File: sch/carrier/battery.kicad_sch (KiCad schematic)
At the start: 2 parts

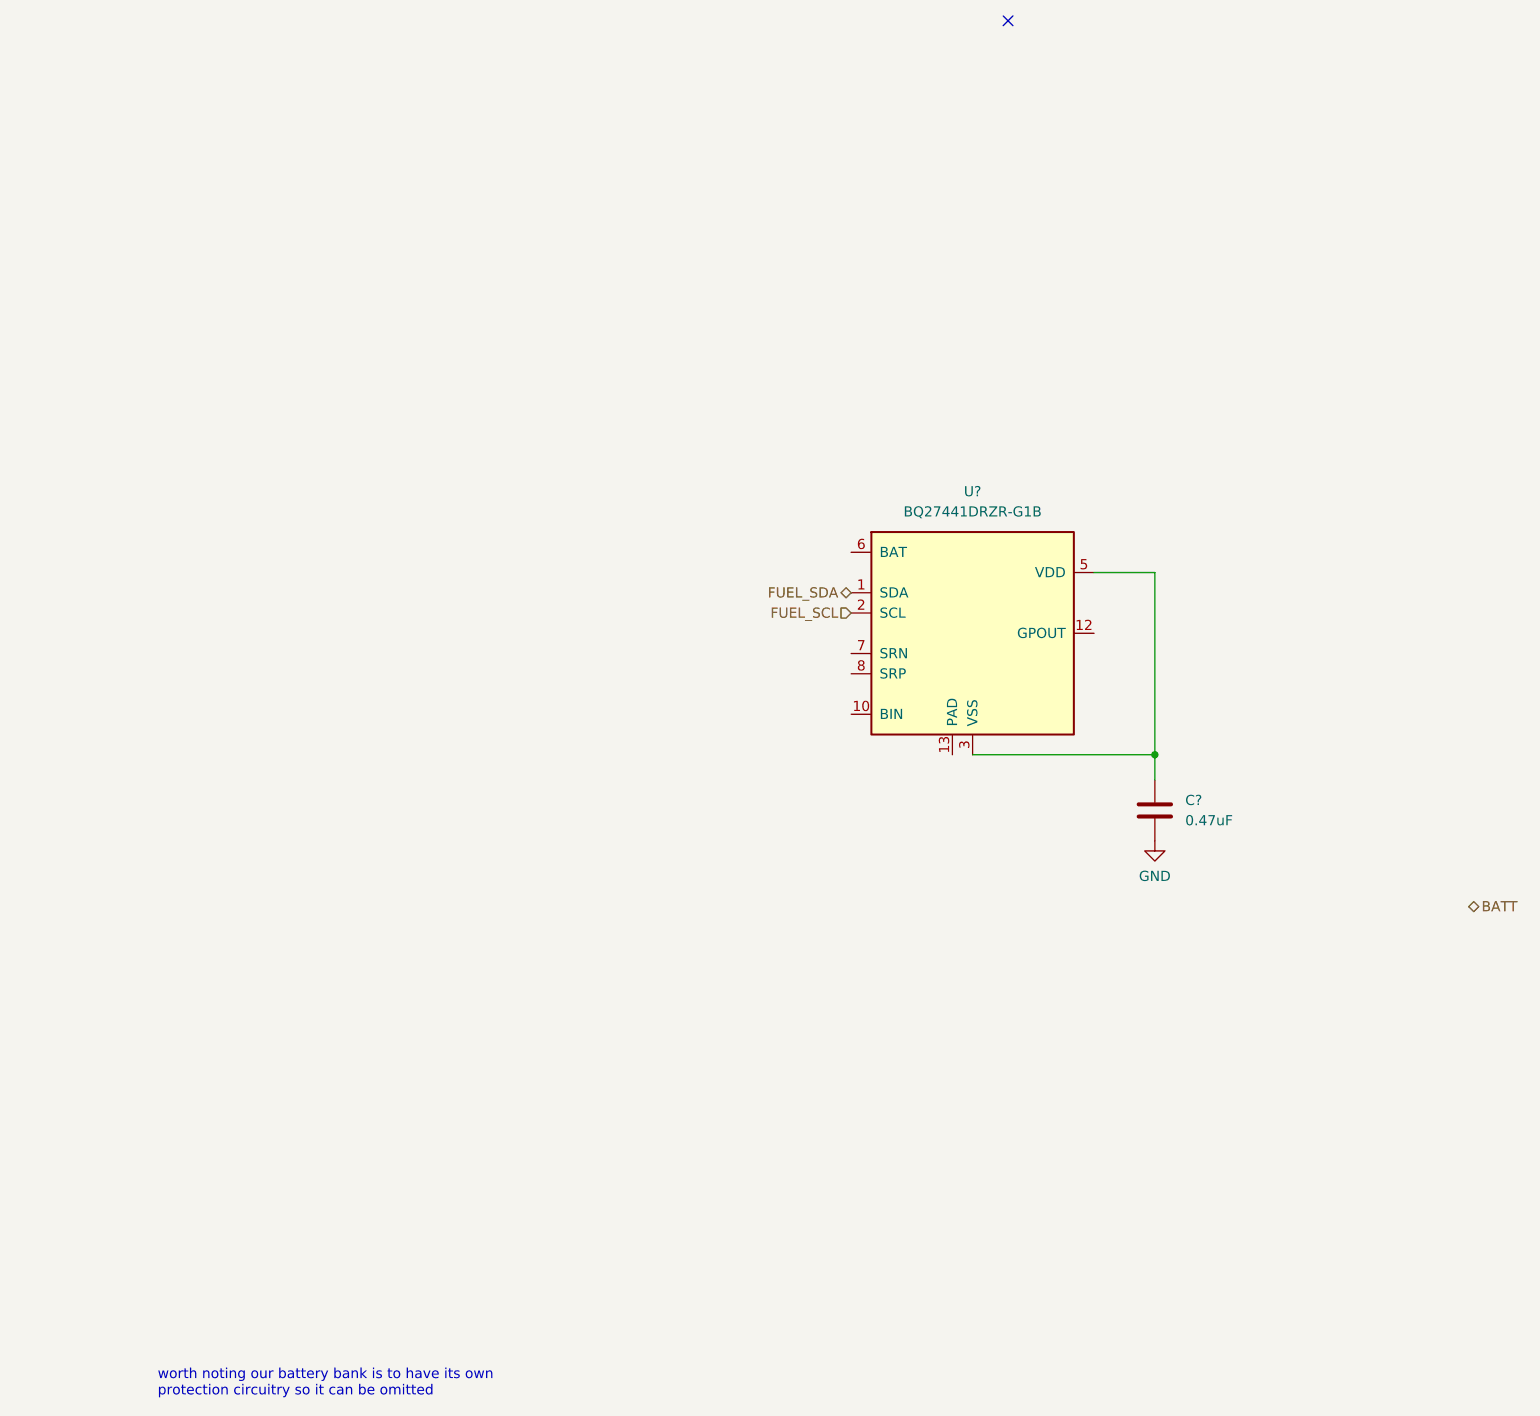
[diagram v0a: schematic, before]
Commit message: add speaker and charger
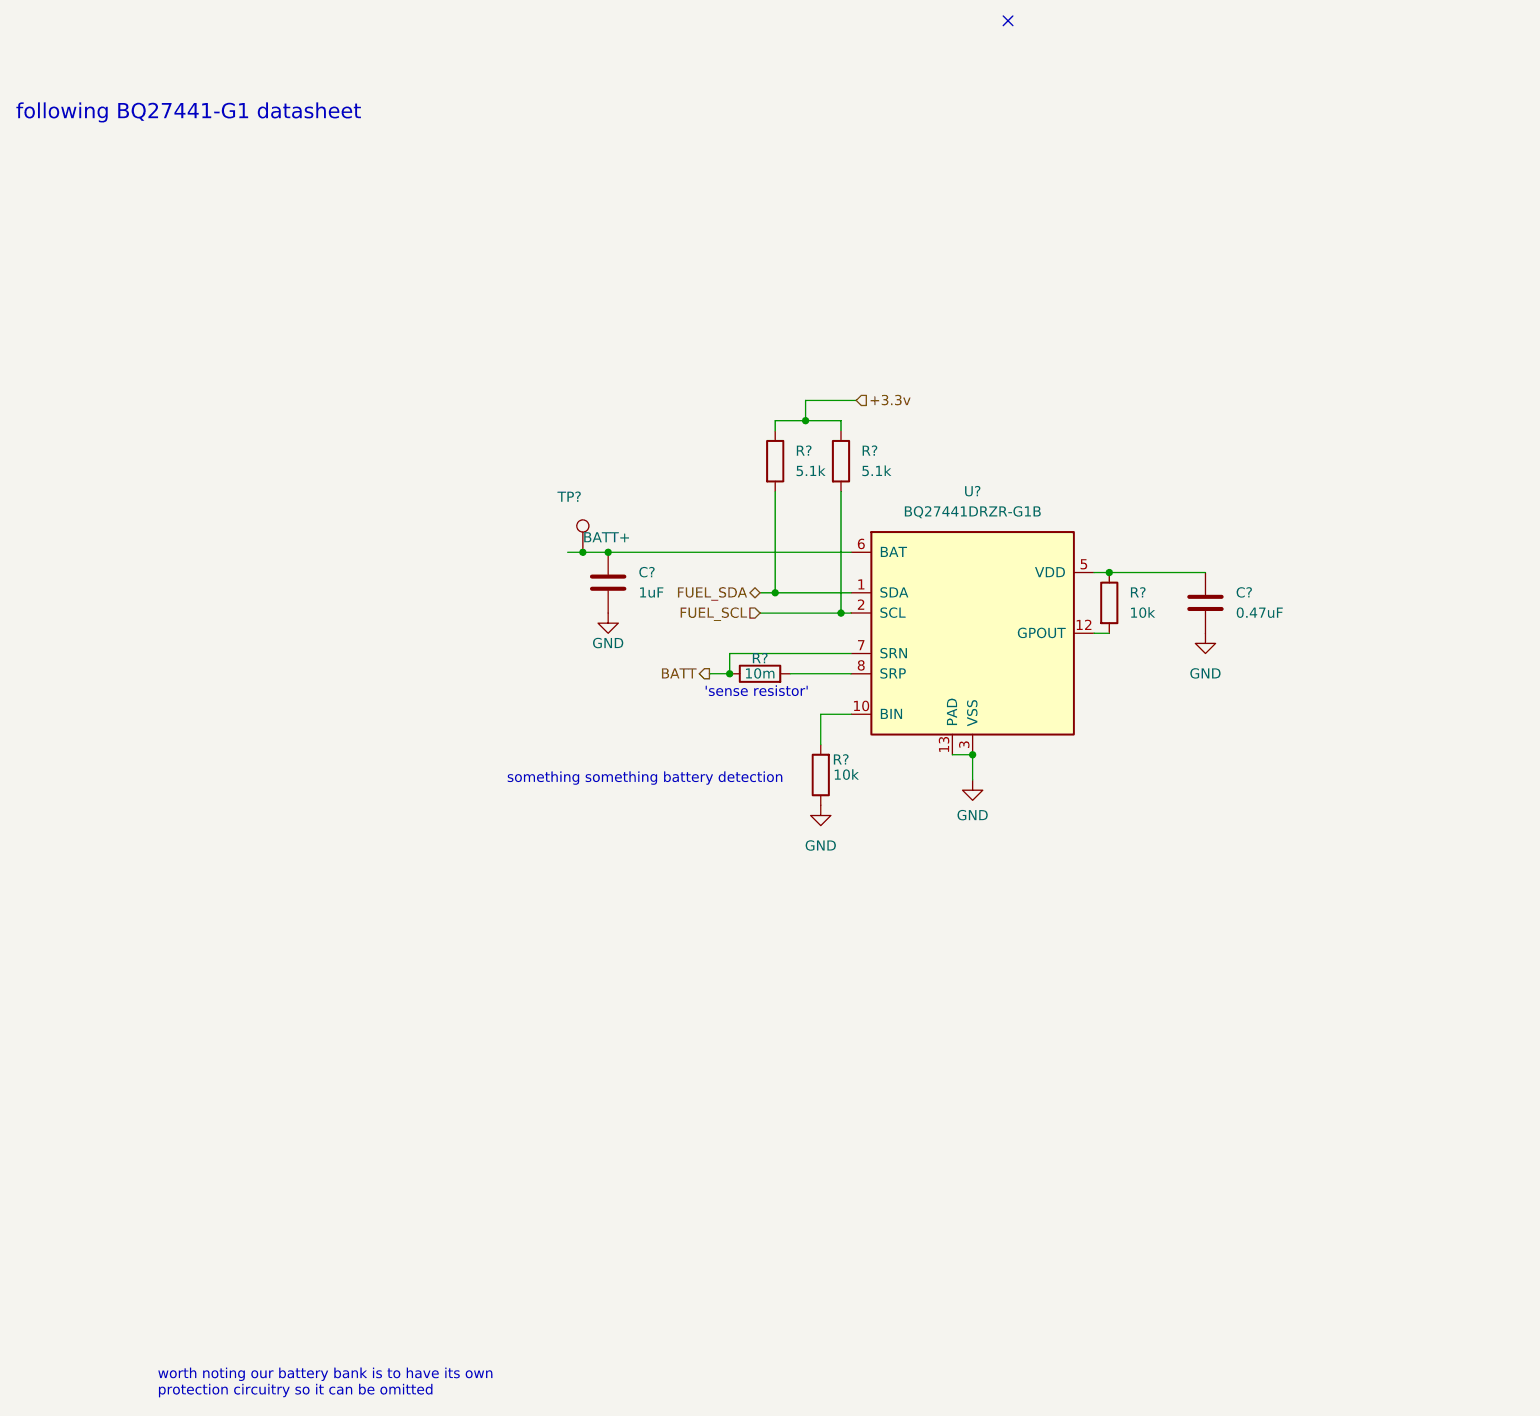
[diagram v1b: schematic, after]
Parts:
- added C?: 1uF, symbol Device:C
- added R? (x2): 5.1k, symbol Device:R
- added R?: 10m, symbol Device:R
- added R? (x2): 10k, symbol Device:R
- added TP?: BATT+, symbol Connector:TestPoint
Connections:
- net BATT: now also U?.7 (SRN), R?.1
- net FUEL_SCL: now also R?.2
- net FUEL_SDA: now also R?.2
- net GND: now also U?.13 (PAD), U?.3 (VSS), C?.2, R?.1
- net at C?.1, U?.5 (VDD): now also R?.1; no longer U?.3 (VSS)
- net at U?.10 (BIN): now also R?.2
- net at U?.12 (GPOUT): now also R?.2
- net at U?.6 (BAT): now also C?.1, TP?.1
- net at U?.8 (SRP): now also R?.2
- new net +3.3v: R?.1, R?.1
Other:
- note added: "'sense resistor'"
- note added: "following BQ27441-G1 datasheet"
- note added: "something something battery detection"
- moved on the sheet: C?

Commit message: push updates
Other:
- moved on the sheet: TP?
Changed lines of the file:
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@@
     (comment 1 "https://www.github.com/cinnamondev/gamepithing")
   )
-  (junction (at 92.71 72.39) (diameter 0.9144) (color 0 0 0 0))
+  (junction (at 92.075 72.39) (diameter 0.9144) (color 0 0 0 0))
   (junction (at 95.885 72.39) (diameter 0.9144) (color 0 0 0 0))
   (junction (at 111.125 87.63) (diameter 0.9144) (color 0 0 0 0))
@@
   (junction (at 158.75 74.93) (diameter 0.9144) (color 0 0 0 0))
   (no_connect (at 146.05 5.715))
-  (wire (pts (xy 90.805 72.39) (xy 92.71 72.39))
+  (wire (pts (xy 90.805 72.39) (xy 92.075 72.39))
     (stroke (width 0) (type solid) (color 0 0 0 0))
   )
-  (wire (pts (xy 92.71 72.39) (xy 95.885 72.39))
+  (wire (pts (xy 92.075 72.39) (xy 95.885 72.39))
     (stroke (width 0) (type solid) (color 0 0 0 0))
   )
@@
     (effects (font (size 1.27 1.27)) (justify left))
   )
-  (symbol (lib_id "Connector:TestPoint") (at 92.71 72.39 0) (unit 1)
+  (symbol (lib_id "Connector:TestPoint") (at 92.075 72.39 0) (unit 1)
     (in_bom yes) (on_board yes)
-    (property "Reference" "TP?" (id 0) (at 89.535 65.4684 0)
+    (property "Reference" "TP?" (id 0) (at 88.9 65.4684 0)
       (effects (font (size 1.27 1.27)) (justify left))
     )
-    (property "Value" "BATT+" (id 1) (at 92.71 70.5484 0)
+    (property "Value" "BATT+" (id 1) (at 92.075 70.5484 0)
       (effects (font (size 1.27 1.27)) (justify left))
     )
-    (property "Footprint" "" (id 2) (at 97.79 72.39 0)
+    (property "Footprint" "" (id 2) (at 97.155 72.39 0)
       (effects (font (size 1.27 1.27)) hide)
     )
-    (property "Datasheet" "~" (id 3) (at 97.79 72.39 0)
+    (property "Datasheet" "~" (id 3) (at 97.155 72.39 0)
       (effects (font (size 1.27 1.27)) hide)
     )

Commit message: git pushed
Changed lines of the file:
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@@
     (title "Power and battery")
     (rev "indev")
-    (comment 1 "https://www.github.com/cinnamondev/gamepithing")
   )
   (junction (at 92.075 72.39) (diameter 0.9144) (color 0 0 0 0))
@@
     (effects (font (size 1.27 1.27)) (justify left bottom))
   )
-  (hierarchical_label "BATT" (shape output) (at 108.585 87.63 180)
+  (hierarchical_label "BATT" (shape bidirectional) (at 108.585 87.63 180)
     (effects (font (size 1.27 1.27)) (justify right))
   )

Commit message: we're abt ready to do pcb i hope!
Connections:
- net BATT: now also R?.2; no longer R?.1
- net at C?.1, TP?.1, U?.6 (BAT): now also R?.1, U?.8 (SRP)
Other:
- moved on the sheet: R?
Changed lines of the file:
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@@
   (junction (at 92.075 72.39) (diameter 0.9144) (color 0 0 0 0))
   (junction (at 95.885 72.39) (diameter 0.9144) (color 0 0 0 0))
-  (junction (at 111.125 87.63) (diameter 0.9144) (color 0 0 0 0))
+  (junction (at 103.505 72.39) (diameter 0.9144) (color 0 0 0 0))
+  (junction (at 110.49 85.09) (diameter 0.9144) (color 0 0 0 0))
+  (junction (at 110.49 92.71) (diameter 0.9144) (color 0 0 0 0))
   (junction (at 116.84 77.47) (diameter 0.9144) (color 0 0 0 0))
   (junction (at 120.65 55.88) (diameter 0.9144) (color 0 0 0 0))
@@
     (stroke (width 0) (type solid) (color 0 0 0 0))
   )
-  (wire (pts (xy 95.885 72.39) (xy 126.365 72.39))
-    (stroke (width 0) (type solid) (color 0 0 0 0))
-  )
-  (wire (pts (xy 108.585 87.63) (xy 111.125 87.63))
-    (stroke (width 0) (type solid) (color 0 0 0 0))
-  )
-  (wire (pts (xy 111.125 85.09) (xy 111.125 87.63))
+  (wire (pts (xy 95.885 72.39) (xy 103.505 72.39))
+    (stroke (width 0) (type solid) (color 0 0 0 0))
+  )
+  (wire (pts (xy 103.505 72.39) (xy 126.365 72.39))
+    (stroke (width 0) (type solid) (color 0 0 0 0))
+  )
+  (wire (pts (xy 103.505 92.71) (xy 103.505 72.39))
+    (stroke (width 0) (type solid) (color 0 0 0 0))
+  )
+  (wire (pts (xy 109.855 85.09) (xy 110.49 85.09))
+    (stroke (width 0) (type solid) (color 0 0 0 0))
+  )
+  (wire (pts (xy 110.49 85.09) (xy 126.365 85.09))
+    (stroke (width 0) (type solid) (color 0 0 0 0))
+  )
+  (wire (pts (xy 110.49 92.71) (xy 103.505 92.71))
     (stroke (width 0) (type solid) (color 0 0 0 0))
   )
@@
     (stroke (width 0) (type solid) (color 0 0 0 0))
   )
-  (wire (pts (xy 118.745 87.63) (xy 126.365 87.63))
+  (wire (pts (xy 118.745 87.63) (xy 118.745 92.71))
+    (stroke (width 0) (type solid) (color 0 0 0 0))
+  )
+  (wire (pts (xy 118.745 92.71) (xy 110.49 92.71))
     (stroke (width 0) (type solid) (color 0 0 0 0))
   )
@@
     (stroke (width 0) (type solid) (color 0 0 0 0))
   )
-  (wire (pts (xy 126.365 85.09) (xy 111.125 85.09))
+  (wire (pts (xy 126.365 87.63) (xy 118.745 87.63))
     (stroke (width 0) (type solid) (color 0 0 0 0))
   )
@@
     (effects (font (size 1.27 1.27)) (justify left bottom))
   )
-  (text "'sense resistor'" (at 107.95 90.805 0)
+  (text "'sense resistor'" (at 97.79 96.52 0)
     (effects (font (size 1.27 1.27)) (justify left bottom))
   )
-  (hierarchical_label "BATT" (shape bidirectional) (at 108.585 87.63 180)
+  (hierarchical_label "BATT" (shape bidirectional) (at 109.855 85.09 180)
     (effects (font (size 1.27 1.27)) (justify right))
   )
@@
     (pin "1")
   )
-  (symbol (lib_id "Device:R") (at 114.935 87.63 90) (unit 1)
+  (symbol (lib_id "Device:R") (at 110.49 88.9 180) (unit 1)
     (in_bom yes) (on_board yes)
-    (property "Reference" "R?" (id 0) (at 114.935 85.725 90))
-    (property "Value" "10m" (id 1) (at 114.935 87.63 90))
-    (property "Footprint" "" (id 2) (at 114.935 89.408 90)
-      (effects (font (size 1.27 1.27)) hide)
-    )
-    (property "Datasheet" "~" (id 3) (at 114.935 87.63 0)
-      (effects (font (size 1.27 1.27)) hide)
-    )
+    (property "Reference" "R?" (id 0) (at 108.585 88.9 90))
+    (property "Value" "10m" (id 1) (at 110.49 88.9 90))
+    (property "Footprint" "" (id 2) (at 112.268 88.9 90)
+      (effects (font (size 1.27 1.27)) hide)
+    )
+    (property "Datasheet" "~" (id 3) (at 110.49 88.9 0)
+      (effects (font (size 1.27 1.27)) hide)
+    )

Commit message: ersfdxcv
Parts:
- TP26: renamed from TP?; footprint (none) -> TestPoint:TestPoint_Pad_1.0x1.0mm
- gave numbers to parts that had none: 8
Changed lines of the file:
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@@
   (symbol (lib_id "Connector:TestPoint") (at 92.075 72.39 0) (unit 1)
     (in_bom yes) (on_board yes)
-    (property "Reference" "TP?" (id 0) (at 88.9 65.4684 0)
+    (property "Reference" "TP26" (id 0) (at 88.9 65.4684 0)
       (effects (font (size 1.27 1.27)) (justify left))
     )
@@
       (effects (font (size 1.27 1.27)) (justify left))
     )
-    (property "Footprint" "" (id 2) (at 97.155 72.39 0)
+    (property "Footprint" "TestPoint:TestPoint_Pad_1.0x1.0mm" (id 2) (at 97.155 72.39 0)
       (effects (font (size 1.27 1.27)) hide)
     )
@@
   (symbol (lib_id "power:GND") (at 95.885 80.01 0) (unit 1)
     (in_bom yes) (on_board yes)
-    (property "Reference" "#PWR?" (id 0) (at 95.885 86.36 0)
+    (property "Reference" "#PWR048" (id 0) (at 95.885 86.36 0)
       (effects (font (size 1.27 1.27)) hide)
     )
@@
   (symbol (lib_id "power:GND") (at 122.555 104.14 0) (unit 1)
     (in_bom yes) (on_board yes) (fields_autoplaced)
-    (property "Reference" "#PWR?" (id 0) (at 122.555 110.49 0)
+    (property "Reference" "#PWR049" (id 0) (at 122.555 110.49 0)
       (effects (font (size 1.27 1.27)) hide)
     )
@@
   (symbol (lib_id "power:GND") (at 141.605 100.965 0) (unit 1)
     (in_bom yes) (on_board yes) (fields_autoplaced)
-    (property "Reference" "#PWR?" (id 0) (at 141.605 107.315 0)
+    (property "Reference" "#PWR050" (id 0) (at 141.605 107.315 0)
       (effects (font (size 1.27 1.27)) hide)
     )
@@
   (symbol (lib_id "power:GND") (at 170.815 82.55 0) (unit 1)
     (in_bom yes) (on_board yes) (fields_autoplaced)
-    (property "Reference" "#PWR?" (id 0) (at 170.815 88.9 0)
+    (property "Reference" "#PWR051" (id 0) (at 170.815 88.9 0)
       (effects (font (size 1.27 1.27)) hide)
     )
@@
   (symbol (lib_id "Device:R") (at 110.49 88.9 180) (unit 1)
     (in_bom yes) (on_board yes)
-    (property "Reference" "R?" (id 0) (at 108.585 88.9 90))
+    (property "Reference" "R59" (id 0) (at 108.585 88.9 90))
     (property "Value" "10m" (id 1) (at 110.49 88.9 90))
     (property "Footprint" "" (id 2) (at 112.268 88.9 90)
@@
   (symbol (lib_id "Device:R") (at 116.84 60.96 0) (unit 1)
     (in_bom yes) (on_board yes) (fields_autoplaced)
-    (property "Reference" "R?" (id 0) (at 119.38 59.6899 0)
+    (property "Reference" "R60" (id 0) (at 119.38 59.6899 0)
       (effects (font (size 1.27 1.27)) (justify left))
     )
@@
   (symbol (lib_id "Device:R") (at 122.555 100.33 180) (unit 1)
     (in_bom yes) (on_board yes)
-    (property "Reference" "R?" (id 0) (at 125.095 98.425 0))
+    (property "Reference" "R61" (id 0) (at 125.095 98.425 0))
     (property "Value" "10k" (id 1) (at 125.73 100.33 0))
     (property "Footprint" "" (id 2) (at 124.333 100.33 90)
@@
   (symbol (lib_id "Device:R") (at 125.095 60.96 0) (unit 1)
     (in_bom yes) (on_board yes) (fields_autoplaced)
-    (property "Reference" "R?" (id 0) (at 127.635 59.6899 0)
+    (property "Reference" "R62" (id 0) (at 127.635 59.6899 0)
       (effects (font (size 1.27 1.27)) (justify left))
     )
@@
   (symbol (lib_id "Device:R") (at 158.75 78.74 0) (unit 1)
     (in_bom yes) (on_board yes) (fields_autoplaced)
-    (property "Reference" "R?" (id 0) (at 161.29 77.4699 0)
+    (property "Reference" "R63" (id 0) (at 161.29 77.4699 0)
       (effects (font (size 1.27 1.27)) (justify left))
     )
@@
   (symbol (lib_id "Device:C") (at 95.885 76.2 0) (unit 1)
     (in_bom yes) (on_board yes) (fields_autoplaced)
-    (property "Reference" "C?" (id 0) (at 99.695 74.9299 0)
+    (property "Reference" "C21" (id 0) (at 99.695 74.9299 0)
       (effects (font (size 1.27 1.27)) (justify left))
     )
@@
   (symbol (lib_id "Device:C") (at 170.815 78.74 0) (unit 1)
     (in_bom yes) (on_board yes) (fields_autoplaced)
-    (property "Reference" "C?" (id 0) (at 174.625 77.4699 0)
+    (property "Reference" "C22" (id 0) (at 174.625 77.4699 0)
       (effects (font (size 1.27 1.27)) (justify left))
     )
@@
   (symbol (lib_id "Battery_Management:BQ27441DRZR-G1B") (at 141.605 82.55 0) (unit 1)
     (in_bom yes) (on_board yes) (fields_autoplaced)
-    (property "Reference" "U?" (id 0) (at 141.605 64.77 0))
+    (property "Reference" "U5" (id 0) (at 141.605 64.77 0))
     (property "Value" "BQ27441DRZR-G1B" (id 1) (at 141.605 67.31 0))
     (property "Footprint" "Package_SON:Texas_S-PDSO-N12" (id 2) (at 147.955 96.52 0)

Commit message: a
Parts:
- R59, R63: footprint (none) -> Resistor_SMD:R_0603_1608Metric_Pad0.98x0.95mm_HandSolder
- R60, R61, R62: footprint (none) -> Resistor_SMD:R_0402_1005Metric_Pad0.72x0.64mm_HandSolder
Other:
- note added: "(Current) sense resistors are low value low tolerance resistors https://blog.ttelectronics.com/current-sense-resistors"
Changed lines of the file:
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@@
+    (stroke (width 0) (type solid) (color 0 0 0 0))
+  )
+  (wire (pts (xy 103.505 72.39) (xy 103.505 93.98))
     (stroke (width 0) (type solid) (color 0 0 0 0))
   )
@@
     (stroke (width 0) (type solid) (color 0 0 0 0))
   )
-  (wire (pts (xy 103.505 92.71) (xy 103.505 72.39))
+  (wire (pts (xy 103.505 93.98) (xy 110.49 93.98))
     (stroke (width 0) (type solid) (color 0 0 0 0))
   )
@@
     (stroke (width 0) (type solid) (color 0 0 0 0))
   )
-  (wire (pts (xy 110.49 92.71) (xy 103.505 92.71))
+  (wire (pts (xy 110.49 93.98) (xy 110.49 92.71))
     (stroke (width 0) (type solid) (color 0 0 0 0))
   )
@@
     (effects (font (size 1.905 1.905)) (justify left bottom))
   )
+  (text "(Current) sense resistors are low value low tolerance resistors \nhttps://blog.ttelectronics.com/current-sense-resistors\n"
+    (at 33.02 92.075 0)
+    (effects (font (size 1.27 1.27)) (justify left bottom))
+  )
   (text "worth noting our battery bank is to have its own\nprotection circuitry so it can be omitted"
     (at 39.37 178.435 0)
@@
     (property "Reference" "R59" (id 0) (at 108.585 88.9 90))
     (property "Value" "10m" (id 1) (at 110.49 88.9 90))
-    (property "Footprint" "" (id 2) (at 112.268 88.9 90)
+    (property "Footprint" "Resistor_SMD:R_0603_1608Metric_Pad0.98x0.95mm_HandSolder" (id 2) (at 112.268 88.9 90)
       (effects (font (size 1.27 1.27)) hide)
     )
@@
       (effects (font (size 1.27 1.27)) (justify left))
     )
-    (property "Footprint" "" (id 2) (at 115.062 60.96 90)
+    (property "Footprint" "Resistor_SMD:R_0402_1005Metric_Pad0.72x0.64mm_HandSolder" (id 2) (at 115.062 60.96 90)
       (effects (font (size 1.27 1.27)) hide)
     )
@@
     (property "Reference" "R61" (id 0) (at 125.095 98.425 0))
     (property "Value" "10k" (id 1) (at 125.73 100.33 0))
-    (property "Footprint" "" (id 2) (at 124.333 100.33 90)
+    (property "Footprint" "Resistor_SMD:R_0402_1005Metric_Pad0.72x0.64mm_HandSolder" (id 2) (at 124.333 100.33 90)
       (effects (font (size 1.27 1.27)) hide)
     )
@@
       (effects (font (size 1.27 1.27)) (justify left))
     )
-    (property "Footprint" "" (id 2) (at 123.317 60.96 90)
+    (property "Footprint" "Resistor_SMD:R_0402_1005Metric_Pad0.72x0.64mm_HandSolder" (id 2) (at 123.317 60.96 90)
       (effects (font (size 1.27 1.27)) hide)
     )
@@
       (effects (font (size 1.27 1.27)) (justify left))
     )
-    (property "Footprint" "" (id 2) (at 156.972 78.74 90)
-      (effects (font (size 1.27 1.27)) hide)
-    )
+    (property "Footprint" "Resistor_SMD:R_0603_1608Metric_Pad0.98x0.95mm_HandSolder" (id 2) (at 156.972 78.74 90)
+      (effects (font (size 1.27 1.27)) hide)
+    )
